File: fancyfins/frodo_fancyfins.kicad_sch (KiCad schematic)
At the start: 50 parts, among them J1 TC2050, J4 SWD Header, J5 CFG Header, U16 AZ1117-5.0, U17 W25Q128JVP, U2 MCP2562-E-SN, U3 AZ1117-3.3, U4 STM32F103RCTx, Y1 8MHz 12pF

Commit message: finished layout, added a bunch of footprints, fixed outer form
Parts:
- added J7: ~, fancyfins:card_edge_connector_2x4, symbol Connector_Generic:Conn_02x04_Top_Bottom
- added R5, R6: 10k, symbol Device:R
- J4: footprint Connector_PinHeader_2.54mm:PinHeader_1x04_P2.54mm_Vertical -> (none)
- J5: footprint Connector_PinHeader_2.54mm:PinHeader_1x02_P2.54mm_Vertical -> (none)
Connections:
- net CAN_1_H is gone; now on net CAN_H_IN: R2.1, U2.7 (CANH)
- net CAN_1_L is gone; now on net CAN_L_IN: R2.2, U2.6 (CANL)
- net +3.3V: now also J7.8 (Pin_8), R5.1, R6.1
- net GND: now also J7.3 (Pin_3)
- net P_SCL: now reaches U4.29 (PB10)
- net P_SCL: now also J7.1 (Pin_1), R5.2
- net P_SDA: now reaches U4.30 (PB11)
- net P_SDA: now also J7.2 (Pin_2), R6.2
- net BSY_RADIO: no longer names the net of U4.40 (PC9)
- net RST_RADIO: no longer names the net of U4.39 (PC8)
- no-connect marks 2 -> 6
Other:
- note added: "@TODO make sure that pin numbering is consistent with other part"
- note added: "pressure sensor connector"
- moved on the sheet: J1, R17, R18, R19

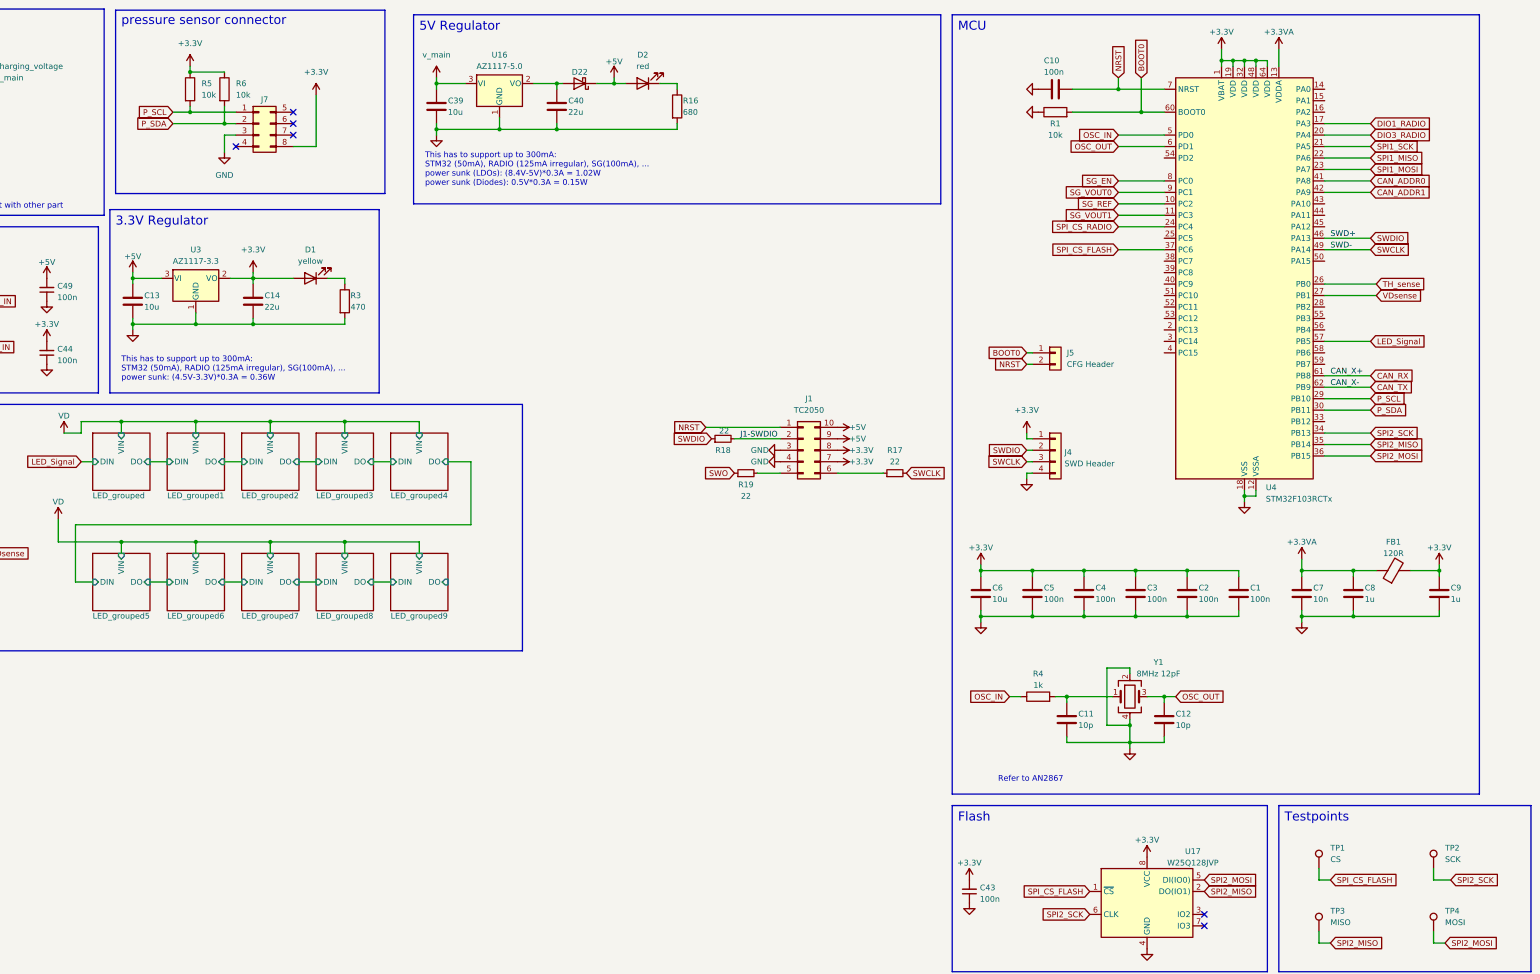
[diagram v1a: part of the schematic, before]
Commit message: changed fancyfins layout a bit; added local footprint library
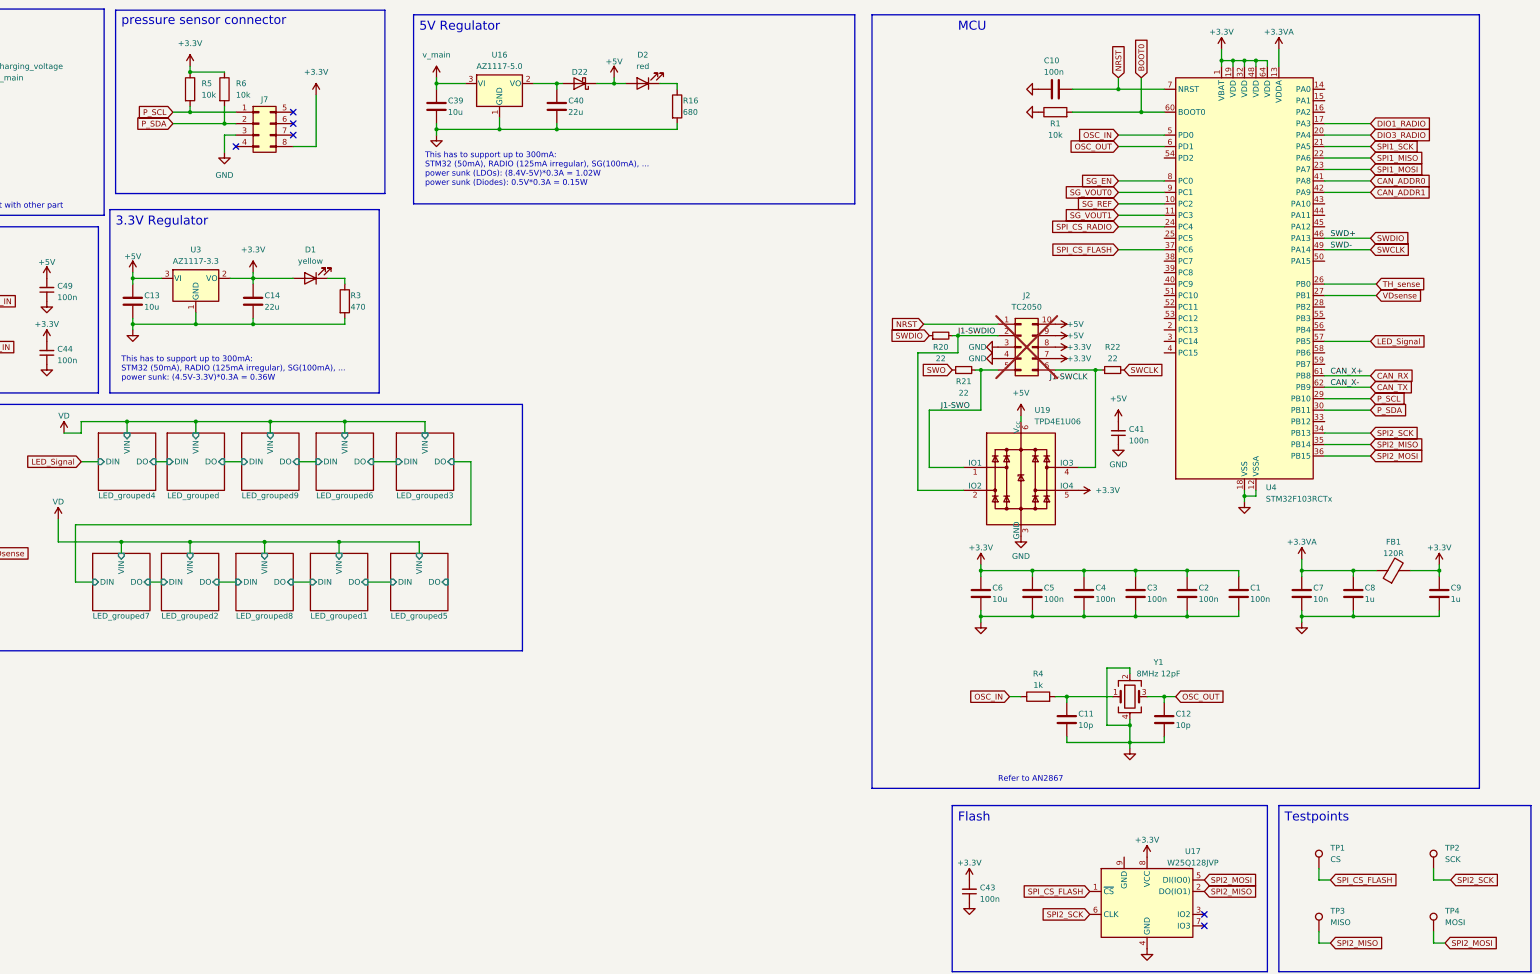
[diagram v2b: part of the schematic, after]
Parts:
- removed J1: TC2050, Connector:Tag-Connect_TC2050-IDC-FP_2x05_P1.27mm_Vertical, symbol Connector_Generic:Conn_02x05_Counter_Clockwise
- removed J4: SWD Header, symbol Connector_Generic:Conn_01x04
- removed J5: CFG Header, symbol Connector_Generic:Conn_01x02
- removed R17, R18, R19: 22, Resistor_SMD:R_0402_1005Metric, symbol Device:R_Small
- added C41: 100n, Capacitor_SMD:C_0402_1005Metric, symbol Device:C_Small
- added J2: TC2050, Connector:Tag-Connect_TC2050-IDC-FP_2x05_P1.27mm_Vertical, symbol Connector_Generic:Conn_02x05_Counter_Clockwise
- added R20, R21, R22: 22, Resistor_SMD:R_0402_1005Metric, symbol Device:R_Small
- added U19: TPD4E1U06, Package_TO_SOT_SMD:SOT-563, symbol stigma:TPD4E001DRL
- R1, R3, R4, R7, R8: footprint Resistor_SMD:R_0402_1005Metric_Pad0.72x0.64mm_HandSolder -> Resistor_SMD:R_0402_1005Metric
- R5, R6: footprint (none) -> Resistor_SMD:R_0402_1005Metric
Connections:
- net +3.3V: now also J2.7 (Pin_7), J2.8 (Pin_8), U19.5 (IO4)
- net +5V: now also C41.2, J2.10 (Pin_10), J2.9 (Pin_9), U19.6 (V_{cc})
- net GND: now also C41.1, J2.3 (Pin_3), J2.4 (Pin_4), U19.3 (GND)
- net J1-SWDIO: now also J2.2 (Pin_2), R20.2, U19.2 (IO2)
- net NRST: now also J2.1 (Pin_1)
- net SWCLK: now also R22.2
- net SWDIO: now also R20.1
- net SWO: now also R21.1
- new net: J2.6 (Pin_6), R22.1, U19.4 (IO3)
- new net J1-SWO: J2.5 (Pin_5), R21.2, U19.1 (IO1)

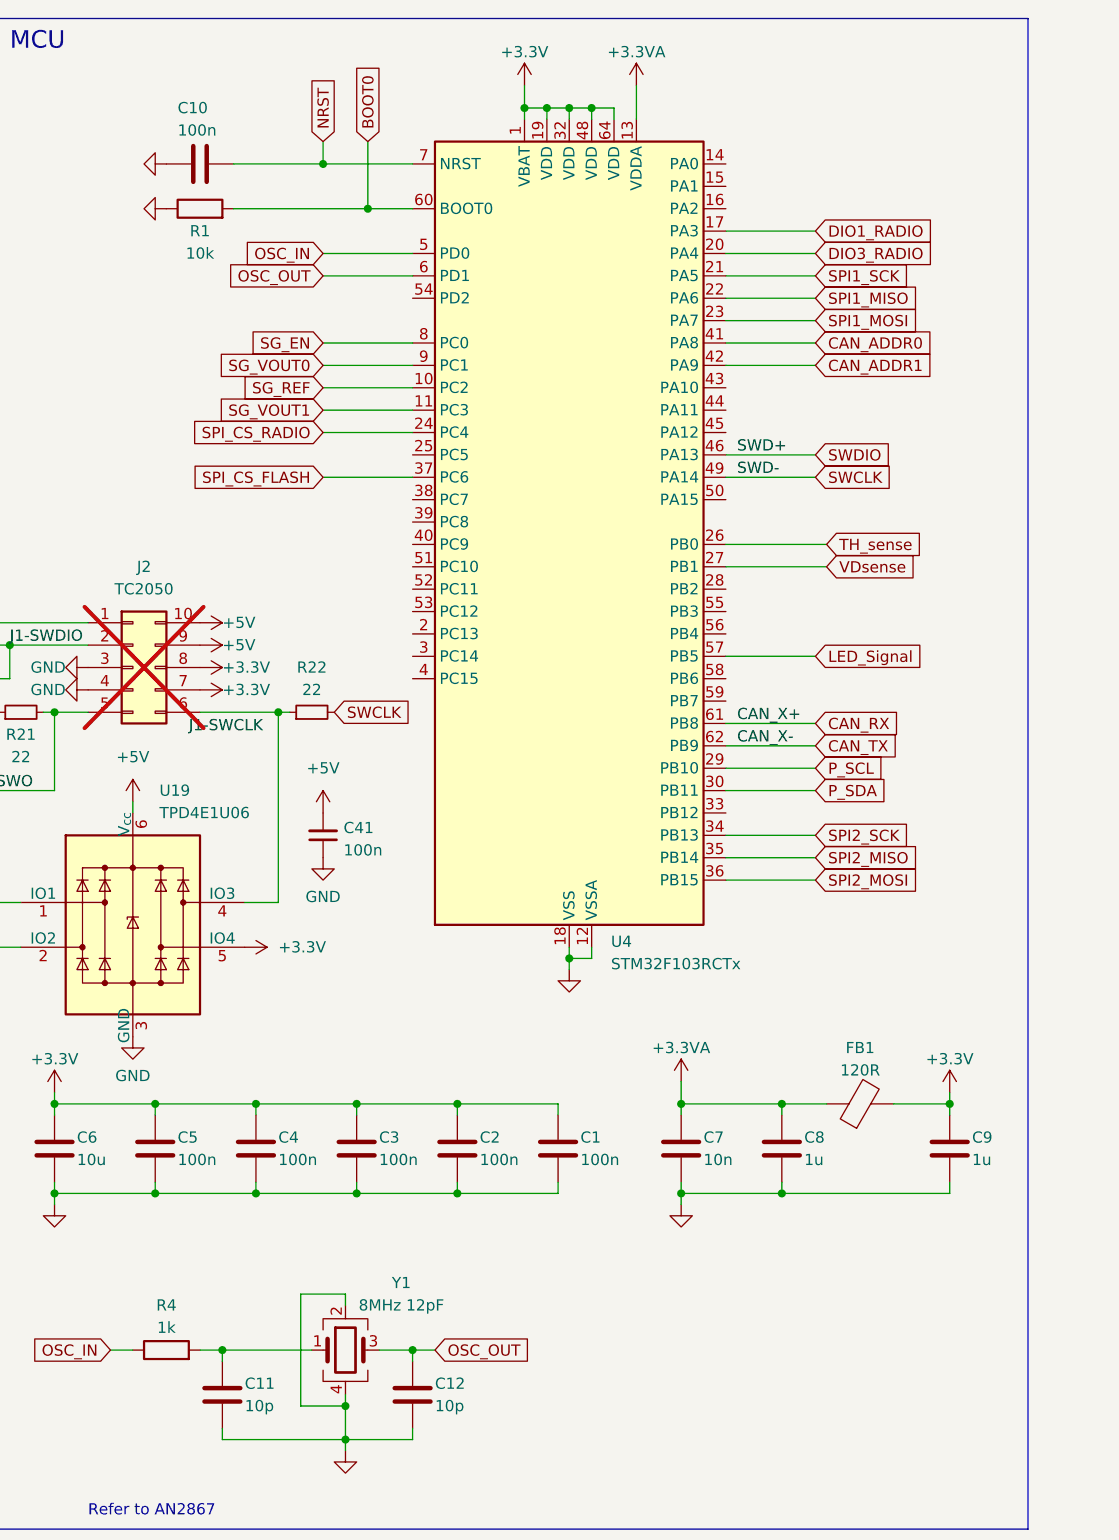
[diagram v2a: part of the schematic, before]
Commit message: added fancy fins routing
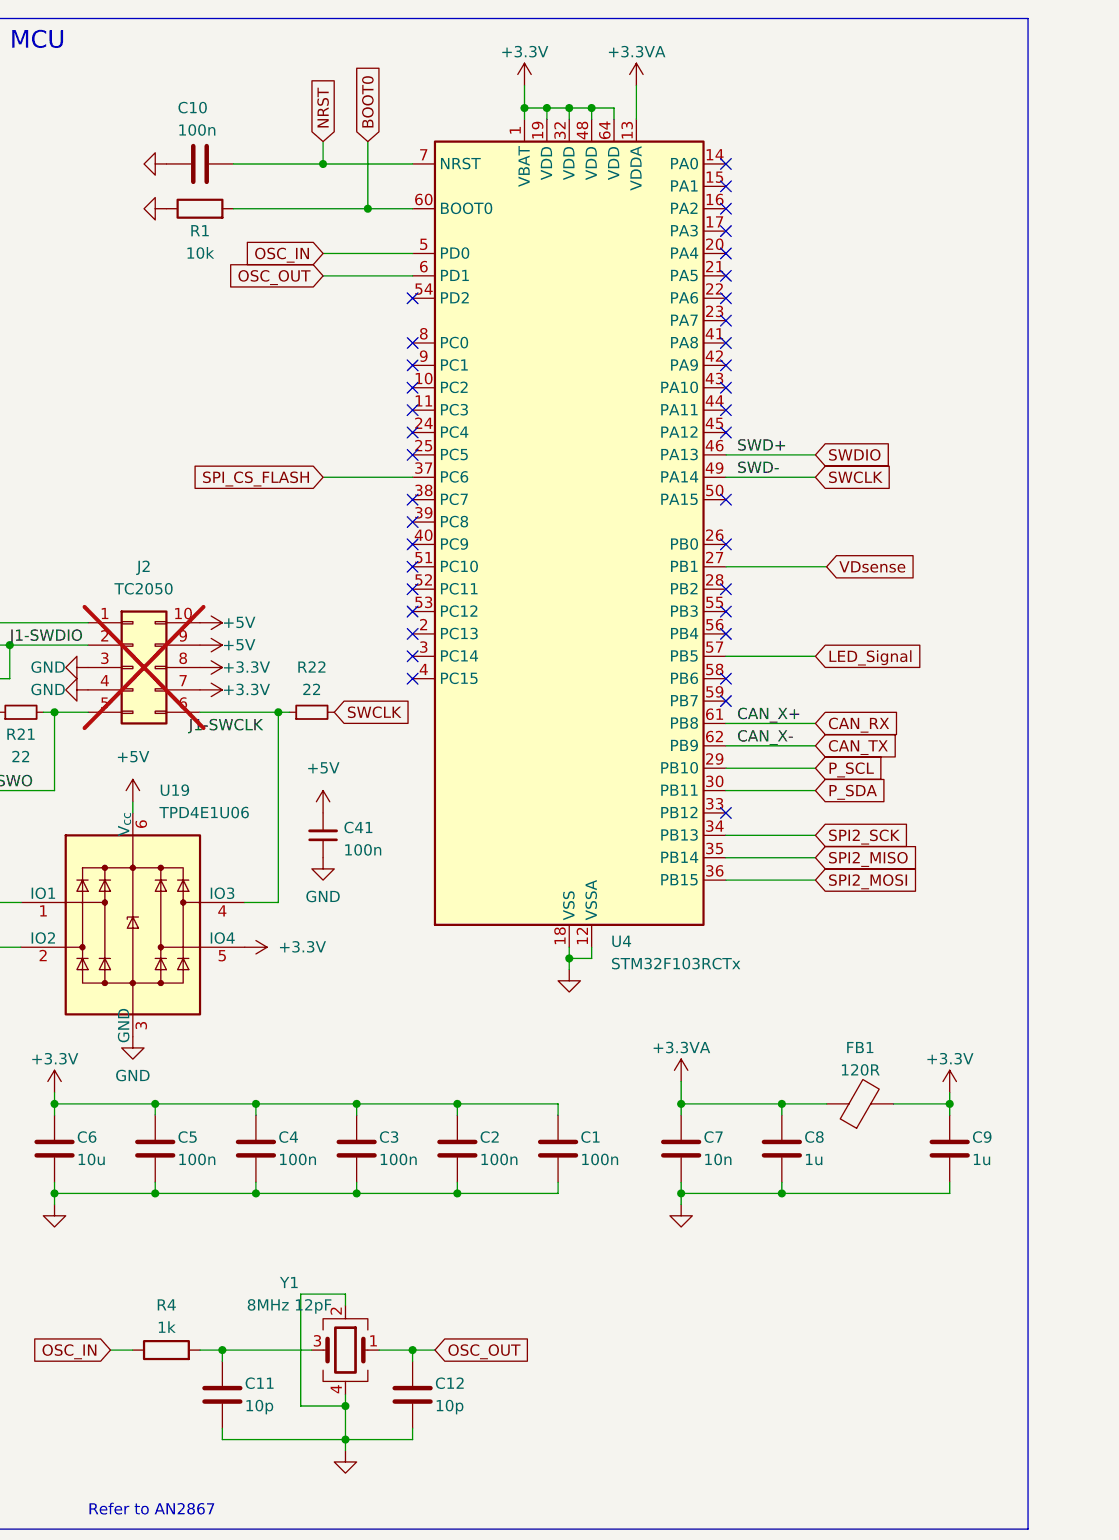
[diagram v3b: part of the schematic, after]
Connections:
- net OSC_OUT: now also Y1.1; no longer Y1.3
- net at C11.1, R4.2: now also Y1.3; no longer Y1.1
- net CAN_ADDR0: no longer names the net of U4.41 (PA8)
- net CAN_ADDR1: no longer names the net of U4.42 (PA9)
- net DIO1_RADIO: no longer names the net of U4.17 (PA3)
- net DIO3_RADIO: no longer names the net of U4.20 (PA4)
- net SG_EN: no longer names the net of U4.8 (PC0)
- net SG_REF: no longer names the net of U4.10 (PC2)
- net SG_VOUT0: no longer names the net of U4.9 (PC1)
- net SG_VOUT1: no longer names the net of U4.11 (PC3)
- net SPI1_MISO: no longer names the net of U4.22 (PA6)
- net SPI1_MOSI: no longer names the net of U4.23 (PA7)
- net SPI1_SCK: no longer names the net of U4.21 (PA5)
- net SPI_CS_RADIO: no longer names the net of U4.24 (PC4)
- net TH_sense: no longer names the net of U4.26 (PB0)
- no-connect marks 6 -> 43

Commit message: fixed led symbol
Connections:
- net GND: now also U17.9 (GND)
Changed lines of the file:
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@@
 	(wire
 		(pts
+			(xy 314.96 196.85) (xy 309.88 196.85)
+		)
+		(stroke
+			(width 0)
+			(type default)
+		)
+	)
+	(wire
+		(pts
 			(xy 124.46 132.08) (xy 140.97 132.08)
 		)
@@
 	(wire
 		(pts
+			(xy 314.96 201.93) (xy 314.96 196.85)
+		)
+		(stroke
+			(width 0)
+			(type default)
+		)
+	)
+	(wire
+		(pts
 			(xy 317.5 138.43) (xy 317.5 139.7)
 		)
@@
 	(wire
 		(pts
+			(xy 309.88 196.85) (xy 309.88 199.39)
+		)
+		(stroke
+			(width 0)
+			(type default)
+		)
+	)
+	(wire
+		(pts
 			(xy 162.56 40.64) (xy 162.56 41.91)
 		)
@@
 					(unit 1)
 				)
+			)
+		)
+	)
+	(symbol
+		(lib_id "power:GND")
+		(at 309.88 199.39 0)
+		(unit 1)
+		(exclude_from_sim no)
+		(in_bom yes)
+		(on_board yes)
+		(dnp no)
+		(fields_autoplaced yes)
+		(property "Reference" "#PWR090"
+			(at 309.88 205.74 0)
+			(effects
+				(font
+					(size 1.27 1.27)
+				)
+				(hide yes)
+			)
+		)
+		(property "Value" "GND"
+			(at 309.88 203.8334 0)
+			(effects
+				(font
+					(size 1.27 1.27)
+				)
+				(hide yes)
+			)
+		)
+		(property "Footprint" ""
+			(at 309.88 199.39 0)
+			(effects
+				(font
+					(size 1.27 1.27)
+				)
+				(hide yes)
+			)
+		)
+		(property "Datasheet" ""
+			(at 309.88 199.39 0)
+			(effects
+				(font
+					(size 1.27 1.27)
+				)
+				(hide yes)
+			)
+		)
+		(property "Description" ""
+			(at 309.88 199.39 0)
+			(effects
+				(font
+					(size 1.27 1.27)
+				)
+			)
+		)
+		(pin "1"
+		)
+		(instances
+			(project "frodo_fancyfins"
+				(path "/6b822b14-450b-45c3-a34b-8e18c5811754"
+					(reference "#PWR090")
+					(unit 1)
+				)

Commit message: changed fancyfinns pcb layout
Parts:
- removed D22: D_Schottky, Diode_SMD:D_SOD-123F, symbol Device:D_Schottky
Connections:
- net +5V: now also C40.1, U16.2 (VO)
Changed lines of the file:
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@@
 	(wire
 		(pts
-			(xy 189.23 30.48) (xy 190.5 30.48)
+			(xy 189.23 30.48) (xy 201.93 30.48)
 		)
 		(stroke
@@
 	(wire
 		(pts
-			(xy 198.12 30.48) (xy 201.93 30.48)
-		)
-		(stroke
-			(width 0)
-			(type default)
-		)
-	)
-	(wire
-		(pts
 			(xy 30.48 26.67) (xy 33.02 26.67)
 		)
@@
 					(unit 1)
 				)
-			)
-		)
-	)
-	(symbol
-		(lib_id "Device:D_Schottky")
-		(at 194.31 30.48 180)
-		(unit 1)
-		(exclude_from_sim no)
-		(in_bom yes)
-		(on_board yes)
-		(dnp no)
-		(property "Reference" "D22"
-			(at 194.31 27.94 0)
-			(effects
-				(font
-					(size 1.27 1.27)
-				)
-			)
-		)
-		(property "Value" "D_Schottky"
-			(at 194.31 27.94 0)
-			(effects
-				(font
-					(size 1.27 1.27)
-				)
-				(hide yes)
-			)
-		)
-		(property "Footprint" "Diode_SMD:D_SOD-123F"
-			(at 194.31 30.48 0)
-			(effects
-				(font
-					(size 1.27 1.27)
-				)
-				(hide yes)
-			)
-		)
-		(property "Datasheet" "~"
-			(at 194.31 30.48 0)
-			(effects
-				(font
-					(size 1.27 1.27)
-				)
-				(hide yes)
-			)
-		)
-		(property "Description" ""
-			(at 194.31 30.48 0)
-			(effects
-				(font
-					(size 1.27 1.27)
-				)
-			)
-		)
-		(property "Notes" ""
-			(at 194.31 30.48 0)
-			(effects
-				(font
-					(size 1.27 1.27)
-				)
-				(hide yes)
-			)
-		)
-		(property "LCSC#" "C167645"
-			(at 194.31 30.48 0)
-			(effects
-				(font
-					(size 1.27 1.27)
-				)
-				(hide yes)
-			)
-		)
-		(pin "2"
-		)
-		(pin "1"
-		)
-		(instances
-			(project "frodo_fancyfins"
-				(path "/6b822b14-450b-45c3-a34b-8e18c5811754"
-					(reference "D22")
-					(unit 1)
-				)

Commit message: changed led routing
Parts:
- added C18, C20, C22, C24, C26, C31, C33, C35, C37, C39: 330n, Capacitor_SMD:C_0402_1005Metric, symbol Device:C
- added C19, C21, C23, C25, C27, C32, C34, C36, C38, C40: 100n, Capacitor_SMD:C_0402_1005Metric, symbol Device:C
- added D10, D11, D12, D13, D14, D15, D16, D17, D18, D19, D20, D21, D22, D23, D24, D5, D6, D7, D8, D9: 3210, fancyfins:1313210530000, symbol LED:Inolux_IN-PI554FCH
- added U10, U12, U13, U14, U15, U16, U6, U7, U8, U9: L78L05_SOT89, Package_TO_SOT_SMD:SOT-89-3, symbol Regulator_Linear:L78L05_SOT89
- renumbered C10 to C1, C5 to C10, C4 to C11, C3 to C12, C2 to C13, C1 to C14, C7 to C15, C8 to C16, C9 to C17, C39 to C2, C11 to C28, C12 to C29, C40 to C3, C43 to C30, C49 to C4, C13 to C5, C14 to C6, C44 to C7, C41 to C8, C6 to C9, D25 to D1, D1 to D3, D23 to D4, J6 to J1, J7 to J2, J2 to J3, R5 to R1, R8 to R10, R7 to R11, R4 to R12, R6 to R2, R16 to R3, R1 to R4, R3 to R5, R2 to R6, R20 to R7, R21 to R8, R22 to R9, U16 to U1, U17 to U11, U3 to U2, U4 to U3, U2 to U4, U19 to U5
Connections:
- net GND: now also C18.2, C19.2, C20.2, C21.2, C22.2, C23.2, C24.2, C25.2, C26.2, C27.2, C31.2, C32.2, C33.2, C34.2, C35.2, C36.2, C37.2, C38.2, C39.2, C40.2, D10.2 (VSS), D11.2 (VSS), D12.2 (VSS), D13.2 (VSS), D14.2 (VSS), D15.2 (VSS), D16.2 (VSS), D17.2 (VSS), D18.2 (VSS), D19.2 (VSS), D20.2 (VSS), D21.2 (VSS), D22.2 (VSS), D23.2 (VSS), D24.2 (VSS), D5.2 (VSS), D6.2 (VSS), D7.2 (VSS), D8.2 (VSS), D9.2 (VSS), U10.2 (GND), U12.2 (GND), U13.2 (GND), U14.2 (GND), U15.2 (GND), U16.2 (GND), U6.2 (GND), U7.2 (GND), U8.2 (GND), U9.2 (GND)
- net LED_Signal: now also D5.4 (DIN)
- net VD: now also C18.1, C20.1, C22.1, C24.1, C26.1, C31.1, C33.1, C35.1, C37.1, C39.1, U10.3 (IN), U12.3 (IN), U13.3 (IN), U14.3 (IN), U15.3 (IN), U16.3 (IN), U6.3 (IN), U7.3 (IN), U8.3 (IN), U9.3 (IN)
- new net: C25.1, D11.3 (VDD), D12.3 (VDD), U9.1 (OUT)
- new net: C32.1, D15.3 (VDD), D16.3 (VDD), U12.1 (OUT)
- new net: D7.1 (DO), D8.4 (DIN)
- new net: C21.1, D7.3 (VDD), D8.3 (VDD), U7.1 (OUT)
- new net: D6.1 (DO), D7.4 (DIN)
- new net: D17.1 (DO), D18.4 (DIN)
- new net: C34.1, D17.3 (VDD), D18.3 (VDD), U13.1 (OUT)
- new net: D16.1 (DO), D17.4 (DIN)
- new net: D13.1 (DO), D14.4 (DIN)
- new net: C27.1, D13.3 (VDD), D14.3 (VDD), U10.1 (OUT)
- new net: D12.1 (DO), D13.4 (DIN)
- new net: D15.1 (DO), D16.4 (DIN)
- new net: D11.1 (DO), D12.4 (DIN)
- new net: D5.1 (DO), D6.4 (DIN)
- new net: C19.1, D5.3 (VDD), D6.3 (VDD), U6.1 (OUT)
- new net: D10.4 (DIN), D9.1 (DO)
- new net: C23.1, D10.3 (VDD), D9.3 (VDD), U8.1 (OUT)
- new net: D8.1 (DO), D9.4 (DIN)
- new net: C40.1, D23.3 (VDD), D24.3 (VDD), U16.1 (OUT)
- new net: D23.1 (DO), D24.4 (DIN)
- new net: D19.1 (DO), D20.4 (DIN)
- new net: C36.1, D19.3 (VDD), D20.3 (VDD), U14.1 (OUT)
- new net: D18.1 (DO), D19.4 (DIN)
- new net: C38.1, D21.3 (VDD), D22.3 (VDD), U15.1 (OUT)
- new net: D10.1 (DO), D11.4 (DIN)
- new net: D21.1 (DO), D22.4 (DIN)
- new net: D20.1 (DO), D21.4 (DIN)
- new net: D22.1 (DO), D23.4 (DIN)
- new net LED_Signal_cont: D14.1 (DO), D15.4 (DIN)
- no-connect marks 43 -> 44
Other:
- removed sheet LED_grouped
- removed sheet LED_grouped1
- removed sheet LED_grouped2
- removed sheet LED_grouped3
- removed sheet LED_grouped4
- removed sheet LED_grouped5
- removed sheet LED_grouped6
- removed sheet LED_grouped7
- removed sheet LED_grouped8
- removed sheet LED_grouped9
- moved on the sheet: C1, C10, C11, C12, C13, C14, C15, C16, C17, C28, C29, C8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
